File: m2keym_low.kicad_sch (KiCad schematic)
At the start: 14 parts, among them J5 Bus_M.2_MDT180M03001

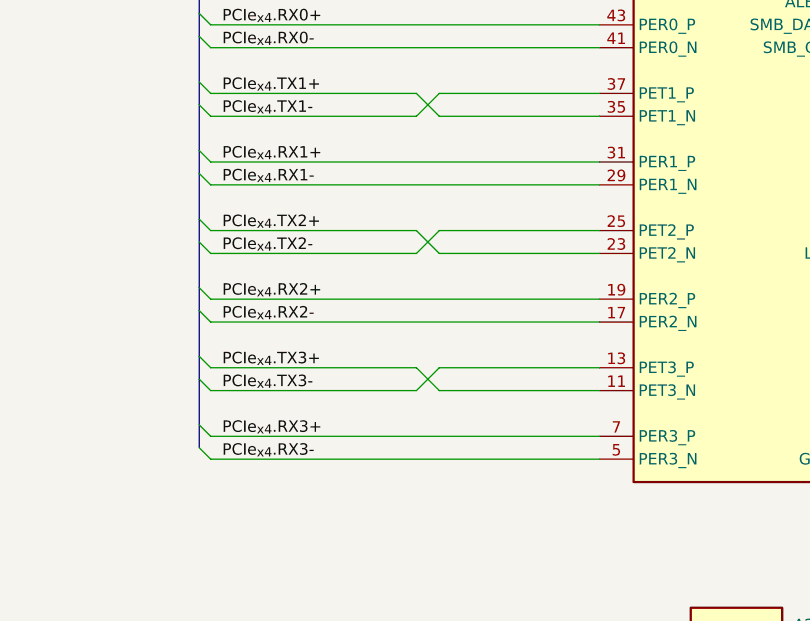
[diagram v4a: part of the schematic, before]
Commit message: [#65840] Reroute PCIe lines near COM connector, to fit GND vias
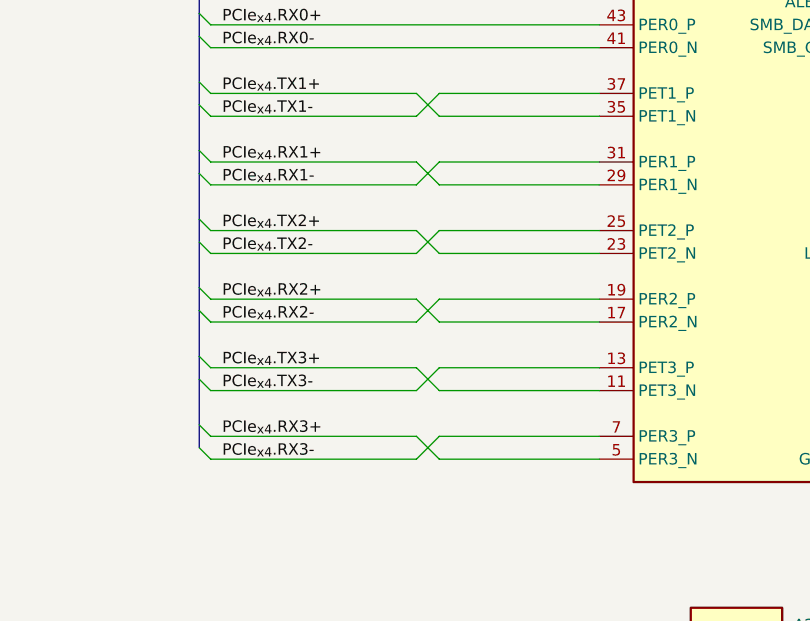
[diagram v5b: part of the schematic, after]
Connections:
- net PCIe_{x4}.RX1+: now also J5.29 (PER1_N); no longer J5.31 (PER1_P)
- net PCIe_{x4}.RX1-: now also J5.31 (PER1_P); no longer J5.29 (PER1_N)
- net PCIe_{x4}.RX2+: now also J5.17 (PER2_N); no longer J5.19 (PER2_P)
- net PCIe_{x4}.RX2-: now also J5.19 (PER2_P); no longer J5.17 (PER2_N)
- net PCIe_{x4}.RX3+: now also J5.5 (PER3_N); no longer J5.7 (PER3_P)
- net PCIe_{x4}.RX3-: now also J5.7 (PER3_P); no longer J5.5 (PER3_N)
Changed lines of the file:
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@@
-    (stroke (width 0) (type default))
-  )
-  (wire (pts (xy 200.66 135.89) (xy 157.48 135.89))
     (stroke (width 0) (type default))
   )
@@
     (stroke (width 0) (type default))
   )
-  (wire (pts (xy 200.66 151.13) (xy 157.48 151.13))
-    (stroke (width 0) (type default))
-  )
   (wire (pts (xy 247.65 92.71) (xy 247.65 91.44))
     (stroke (width 0) (type default))
@@
     (stroke (width 0) (type default))
   )
+  (wire (pts (xy 157.48 148.59) (xy 180.34 148.59))
+    (stroke (width 0) (type default))
+  )
   (bus (pts (xy 181.61 100.33) (xy 181.61 97.79))
     (stroke (width 0) (type default))
   )
+  (wire (pts (xy 180.34 163.83) (xy 182.88 166.37))
+    (stroke (width 0) (type default))
+  )
   (wire (pts (xy 200.66 118.11) (xy 157.48 118.11))
     (stroke (width 0) (type default))
@@
     (stroke (width 0) (type default))
   )
+  (wire (pts (xy 157.48 163.83) (xy 180.34 163.83))
+    (stroke (width 0) (type default))
+  )
   (wire (pts (xy 200.66 120.65) (xy 157.48 120.65))
     (stroke (width 0) (type default))
   )
+  (wire (pts (xy 200.66 148.59) (xy 182.88 148.59))
+    (stroke (width 0) (type default))
+  )
+  (wire (pts (xy 182.88 166.37) (xy 200.66 166.37))
+    (stroke (width 0) (type default))
+  )
   (bus (pts (xy 156.21 119.38) (xy 156.21 124.46))
     (stroke (width 0) (type default))
@@
     (stroke (width 0) (type default))
   )
+  (wire (pts (xy 182.88 151.13) (xy 200.66 151.13))
+    (stroke (width 0) (type default))
+  )
   (bus (pts (xy 156.21 147.32) (xy 156.21 149.86))
     (stroke (width 0) (type default))
@@
     (stroke (width 0) (type default))
   )
-  (wire (pts (xy 200.66 148.59) (xy 157.48 148.59))
-    (stroke (width 0) (type default))
-  )
   (wire (pts (xy 231.14 166.37) (xy 232.41 166.37))
     (stroke (width 0) (type default))
@@
     (stroke (width 0) (type default))
   )
+  (wire (pts (xy 157.48 166.37) (xy 180.34 166.37))
+    (stroke (width 0) (type default))
+  )
   (wire (pts (xy 237.49 85.09) (xy 237.49 86.36))
     (stroke (width 0) (type default))
@@
     (stroke (width 0) (type default))
   )
+  (wire (pts (xy 157.48 133.35) (xy 180.34 133.35))
+    (stroke (width 0) (type default))
+  )
   (wire (pts (xy 157.48 156.21) (xy 180.34 156.21))
     (stroke (width 0) (type default))
@@
     (stroke (width 0) (type default))
   )
-  (wire (pts (xy 200.66 133.35) (xy 157.48 133.35))
-    (stroke (width 0) (type default))
-  )
   (wire (pts (xy 232.41 129.54) (xy 232.41 130.81))
     (stroke (width 0) (type default))
   )
+  (wire (pts (xy 182.88 133.35) (xy 180.34 135.89))
+    (stroke (width 0) (type default))
+  )
   (wire (pts (xy 149.86 88.9) (xy 162.56 88.9))
     (stroke (width 0) (type default))
   )
+  (wire (pts (xy 157.48 151.13) (xy 180.34 151.13))
+    (stroke (width 0) (type default))
+  )
+  (wire (pts (xy 180.34 133.35) (xy 182.88 135.89))
+    (stroke (width 0) (type default))
+  )
   (bus (pts (xy 156.21 149.86) (xy 156.21 154.94))
     (stroke (width 0) (type default))
   )
+  (wire (pts (xy 182.88 135.89) (xy 200.66 135.89))
+    (stroke (width 0) (type default))
+  )
   (wire (pts (xy 182.88 158.75) (xy 200.66 158.75))
     (stroke (width 0) (type default))
@@
     (stroke (width 0) (type default))
   )
+  (wire (pts (xy 182.88 148.59) (xy 180.34 151.13))
+    (stroke (width 0) (type default))
+  )
   (wire (pts (xy 193.04 81.28) (xy 193.04 82.55))
     (stroke (width 0) (type default))
@@
     (stroke (width 0) (type default))
   )
-  (wire (pts (xy 200.66 166.37) (xy 157.48 166.37))
-    (stroke (width 0) (type default))
-  )
   (wire (pts (xy 200.66 125.73) (xy 182.88 125.73))
     (stroke (width 0) (type default))
@@
     (stroke (width 0) (type default))
   )
+  (wire (pts (xy 157.48 135.89) (xy 180.34 135.89))
+    (stroke (width 0) (type default))
+  )
   (wire (pts (xy 232.41 135.89) (xy 232.41 137.16))
     (stroke (width 0) (type default))
@@
     (stroke (width 0) (type default))
   )
+  (wire (pts (xy 180.34 148.59) (xy 182.88 151.13))
+    (stroke (width 0) (type default))
+  )
   (wire (pts (xy 180.34 125.73) (xy 182.88 128.27))
     (stroke (width 0) (type default))
@@
     (stroke (width 0) (type default))
   )
+  (wire (pts (xy 200.66 163.83) (xy 182.88 163.83))
+    (stroke (width 0) (type default))
+  )
   (wire (pts (xy 232.41 142.24) (xy 232.41 143.51))
     (stroke (width 0) (type default))
   )
+  (wire (pts (xy 182.88 163.83) (xy 180.34 166.37))
+    (stroke (width 0) (type default))
+  )
   (wire (pts (xy 232.41 163.83) (xy 231.14 163.83))
     (stroke (width 0) (type default))
   )
+  (wire (pts (xy 200.66 133.35) (xy 182.88 133.35))
+    (stroke (width 0) (type default))
+  )
   (wire (pts (xy 182.88 156.21) (xy 180.34 158.75))
     (stroke (width 0) (type default))
@@
     (stroke (width 0) (type default))
   )
-  (wire (pts (xy 200.66 163.83) (xy 157.48 163.83))
-    (stroke (width 0) (type default))
-  )

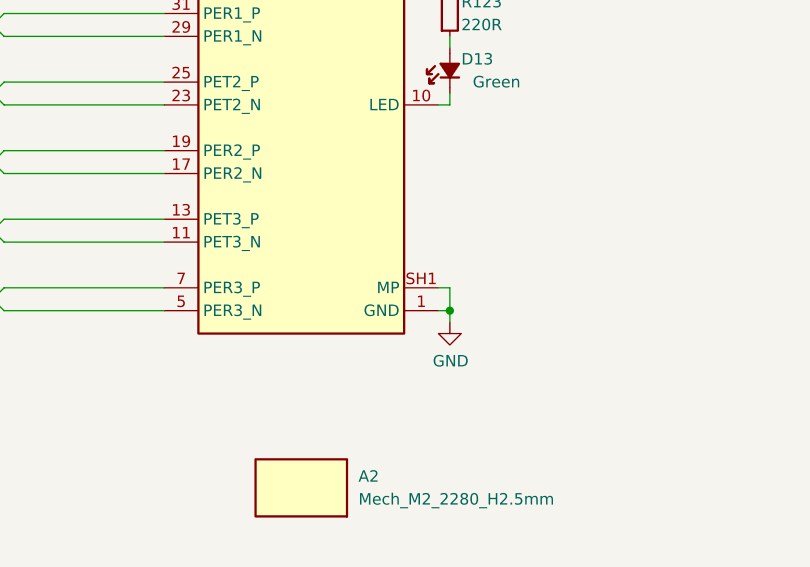
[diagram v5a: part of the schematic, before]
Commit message: [#66613] Update M.2 connector
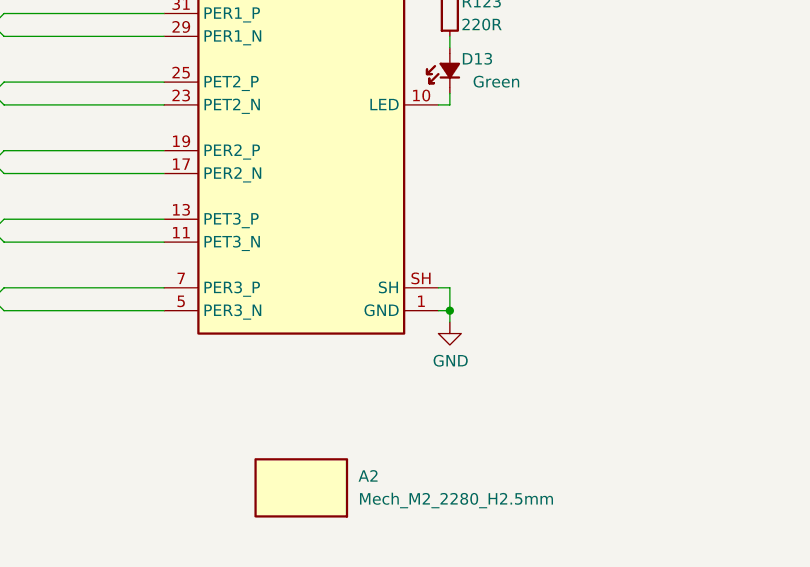
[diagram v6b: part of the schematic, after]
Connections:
- net GND: now also J5.SH; no longer J5.SH1 (MP), J5.SH2 (MP)
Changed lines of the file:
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@@
-    )
-  )
-  (symbol (lib_id "antmicroPciConnectors:Bus_M.2_MDT180M03001") (at 200.66 88.9 0) (unit 1)
-    (in_bom yes) (on_board yes) (dnp no) (fields_autoplaced)
-    (property "Reference" "J5" (at 215.9 81.28 0)
-      (effects (font (size 1.27 1.27) (thickness 0.15)))
-    )
-    (property "Value" "Bus_M.2_MDT180M03001" (at 246.38 96.52 0)
-      (effects (font (size 1.27 1.27) (thickness 0.15)) (justify left bottom) hide)
-    )
-    (property "Footprint" "antmicro-footprints:Bus_M.2_Socket_Key_M_Amphenol_MDT180M03001" (at 246.38 99.06 0)
-      (effects (font (size 1.27 1.27) (thickness 0.15)) (justify left bottom) hide)
-    )
-    (property "Datasheet" "https://cdn.amphenol-cs.com/media/wysiwyg/files/drawing/mdt180xxx001.pdf" (at 246.38 101.6 0)
-      (effects (font (size 1.27 1.27) (thickness 0.15)) (justify left bottom) hide)
-    )
-    (property "Manufacturer" "Amphenol" (at 246.38 104.14 0)
-      (effects (font (size 1.27 1.27) (thickness 0.15)) (justify left bottom) hide)
-    )
-    (property "MPN" "MDT180M03001" (at 215.9 83.82 0)
-      (effects (font (size 1.27 1.27) (thickness 0.15)))
-    )
-    (property "Author" "Antmicro" (at 246.38 106.68 0)
-      (effects (font (size 1.27 1.27) (thickness 0.15)) (justify left bottom) hide)
-    )
-    (property "License" "Apache-2.0" (at 246.38 109.22 0)
-      (effects (font (size 1.27 1.27) (thickness 0.15)) (justify left bottom) hide)
-    )
-    (pin "39")
-    (pin "37")
-    (pin "28")
-    (pin "3")
-    (pin "45")
-    (pin "40")
-    (pin "75")
-    (pin "15")
-    (pin "29")
-    (pin "69")
-    (pin "38")
-    (pin "23")
-    (pin "21")
-    (pin "8")
-    (pin "4")
-    (pin "1")
-    (pin "30")
-    (pin "10")
-    (pin "73")
-    (pin "2")
-    (pin "9")
-    (pin "32")
-    (pin "47")
-    (pin "26")
-    (pin "44")
-    (pin "18")
-    (pin "34")
-    (pin "33")
-    (pin "35")
-    (pin "55")
-    (pin "56")
-    (pin "17")
-    (pin "27")
-    (pin "SH2")
-    (pin "19")
-    (pin "25")
-    (pin "46")
-    (pin "43")
-    (pin "48")
-    (pin "6")
-    (pin "57")
-    (pin "49")
-    (pin "68")
-    (pin "52")
-    (pin "5")
-    (pin "12")
-    (pin "13")
-    (pin "74")
-    (pin "71")
-    (pin "7")
-    (pin "41")
-    (pin "58")
-    (pin "20")
-    (pin "36")
-    (pin "67")
-    (pin "53")
-    (pin "54")
-    (pin "72")
-    (pin "16")
-    (pin "42")
-    (pin "70")
-    (pin "31")
-    (pin "SH1")
-    (pin "11")
-    (pin "14")
-    (pin "24")
-    (pin "51")
-    (pin "22")
-    (pin "50")
-    (instances
-      (project "com-express-7-baseboard"
-        (path "/1b8c34da-dad5-4b0b-8c4b-45db766c4dfa/2acc1b08-bc1c-4714-8c61-ebdd69dbc5a5"
-          (reference "J5") (unit 1)
-        )
-      )
     )
   )
@@
         )
       )
+    )
+  )
+  (symbol (lib_name "Bus_M.2_MDT180M03001_1") (lib_id "antmicroPciConnectors:Bus_M.2_MDT180M03001") (at 200.66 88.9 0) (unit 1)
+    (in_bom yes) (on_board yes) (dnp no) (fields_autoplaced)
+    (property "Reference" "J5" (at 215.9 81.28 0)
+      (effects (font (size 1.27 1.27) (thickness 0.15)))
+    )
+    (property "Value" "Bus_M.2_MDT180M03001" (at 246.38 96.52 0)
+      (effects (font (size 1.27 1.27) (thickness 0.15)) (justify left bottom) hide)
+    )
+    (property "Footprint" "antmicro-footprints:Bus_M.2_Socket_Key_M_Amphenol_MDT180M03001" (at 246.38 99.06 0)
+      (effects (font (size 1.27 1.27) (thickness 0.15)) (justify left bottom) hide)
+    )
+    (property "Datasheet" "https://cdn.amphenol-cs.com/media/wysiwyg/files/drawing/mdt180xxx001.pdf" (at 246.38 101.6 0)
+      (effects (font (size 1.27 1.27) (thickness 0.15)) (justify left bottom) hide)
+    )
+    (property "Manufacturer" "Amphenol" (at 246.38 104.14 0)
+      (effects (font (size 1.27 1.27) (thickness 0.15)) (justify left bottom) hide)
+    )
+    (property "MPN" "MDT180M03001" (at 215.9 83.82 0)
+      (effects (font (size 1.27 1.27) (thickness 0.15)))
+    )
+    (property "Author" "Antmicro" (at 246.38 106.68 0)
+      (effects (font (size 1.27 1.27) (thickness 0.15)) (justify left bottom) hide)
+    )
+    (property "License" "Apache-2.0" (at 246.38 109.22 0)
+      (effects (font (size 1.27 1.27) (thickness 0.15)) (justify left bottom) hide)
+    )
+    (pin "44")
+    (pin "34")
+    (pin "50")
+    (pin "29")
+    (pin "31")
+    (pin "49")
+    (pin "30")
+    (pin "56")
+    (pin "55")
+    (pin "67")
+    (pin "6")
+    (pin "54")
+    (pin "7")
+    (pin "58")
+    (pin "68")
+    (pin "69")
+    (pin "51")
+    (pin "5")
+    (pin "12")
+    (pin "45")
+    (pin "46")
+    (pin "25")
+    (pin "15")
+    (pin "28")
+    (pin "48")
+    (pin "26")
+    (pin "3")
+    (pin "13")
+    (pin "37")
+    (pin "33")
+    (pin "20")
+    (pin "27")
+    (pin "11")
+    (pin "32")
+    (pin "24")
+    (pin "47")
+    (pin "14")
+    (pin "10")
+    (pin "43")
+    (pin "9")
+    (pin "74")
+    (pin "39")
+    (pin "38")
+    (pin "8")
+    (pin "53")
+    (pin "72")
+    (pin "SH")
+    (pin "40")
+    (pin "42")
+    (pin "41")
+    (pin "1")
+    (pin "23")
+    (pin "35")
+    (pin "22")
+    (pin "75")
+    (pin "17")
+    (pin "71")
+    (pin "52")
+    (pin "4")
+    (pin "73")
+    (pin "57")
+    (pin "19")
+    (pin "18")
+    (pin "16")
+    (pin "2")
+    (pin "70")
+    (pin "21")
+    (pin "36")
+    (instances
+      (project "com-express-7-baseboard"
+        (path "/1b8c34da-dad5-4b0b-8c4b-45db766c4dfa/2acc1b08-bc1c-4714-8c61-ebdd69dbc5a5"
+          (reference "J5") (unit 1)
+        )
+      )
